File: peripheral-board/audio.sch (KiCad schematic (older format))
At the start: 4 parts, among them J6001 JACK_TRS_6PINS, U6001 TCA0372, U6002 MCP4011, U6003 MCP4011

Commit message: added audio jack
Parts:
- removed J6001: JACK_TRS_6PINS, symbol JACK_TRS_6PINS
- added J6001: FCR1295, lib:FCR1295, symbol FCR1295
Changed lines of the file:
@@
 $Descr A4 11693 8268
 encoding utf-8
-Sheet 6 10
+Sheet 7 10
 Title ""
 Date ""
@@
 Comment4 ""
 $EndDescr
-$Comp
-L JACK_TRS_6PINS J6001
-U 1 1 5819EF20
-P 6450 1700
-F 0 "J6001" H 6431 2225 50  0000 C CNN
-F 1 "JACK_TRS_6PINS" H 6431 2134 50  0000 C CNN
-F 2 "" H 6550 1550 50  0001 C CNN
-F 3 "" H 6550 1550 50  0000 C CNN
-	1    6450 1700
-	1    0    0    -1
-$EndComp
 $Comp
 L TCA0372 U6001
@@
 	1900 4750 1600 4750
 $Comp
-L GND #PWR028
+L GND #PWR054
 U 1 1 5823647F
 P 3300 3450
-F 0 "#PWR028" H 3300 3200 50  0001 C CNN
+F 0 "#PWR054" H 3300 3200 50  0001 C CNN
 F 1 "GND" H 3305 3277 50  0000 C CNN
 F 2 "" H 3300 3450 50  0000 C CNN
@@
 $EndComp
 $Comp
-L GND #PWR029
+L GND #PWR055
 U 1 1 582364AF
 P 3300 4850
-F 0 "#PWR029" H 3300 4600 50  0001 C CNN
+F 0 "#PWR055" H 3300 4600 50  0001 C CNN
 F 1 "GND" H 3305 4677 50  0000 C CNN
 F 2 "" H 3300 4850 50  0000 C CNN
@@
 $EndComp
 $Comp
-L +3V3 #PWR030
+L +3V3 #PWR056
 U 1 1 582364E9
 P 3300 2350
-F 0 "#PWR030" H 3300 2200 50  0001 C CNN
+F 0 "#PWR056" H 3300 2200 50  0001 C CNN
 F 1 "+3V3" V 3315 2478 50  0000 L CNN
 F 2 "" H 3300 2350 50  0000 C CNN
@@
 $EndComp
 $Comp
-L +3V3 #PWR031
+L +3V3 #PWR057
 U 1 1 58236543
 P 3350 3800
-F 0 "#PWR031" H 3350 3650 50  0001 C CNN
+F 0 "#PWR057" H 3350 3650 50  0001 C CNN
 F 1 "+3V3" V 3365 3928 50  0000 L CNN
 F 2 "" H 3350 3800 50  0000 C CNN
@@
 	4100 2800 4050 2800
 $Comp
-L GND #PWR032
+L GND #PWR058
 U 1 1 58240DA5
 P 4100 3050
-F 0 "#PWR032" H 4100 2800 50  0001 C CNN
+F 0 "#PWR058" H 4100 2800 50  0001 C CNN
 F 1 "GND" H 4105 2877 50  0000 C CNN
 F 2 "" H 4100 3050 50  0000 C CNN
@@
 $EndComp
 $Comp
-L GND #PWR033
+L GND #PWR059
 U 1 1 58240DD7
 P 4100 4450
-F 0 "#PWR033" H 4100 4200 50  0001 C CNN
+F 0 "#PWR059" H 4100 4200 50  0001 C CNN
 F 1 "GND" H 4105 4277 50  0000 C CNN
 F 2 "" H 4100 4450 50  0000 C CNN
@@
 Wire Wire Line
 	4100 3000 4100 3050
+$Comp
+L FCR1295 J6001
+U 1 1 589D4F61
+P 6450 1700
+F 0 "J6001" H 6431 2225 50  0000 C CNN
+F 1 "FCR1295" H 6431 2134 50  0000 C CNN
+F 2 "lib:FCR1295" H -800 400 50  0001 C CNN
+F 3 "" H -800 400 50  0001 C CNN
+	1    6450 1700
+	1    0    0    -1
+$EndComp
 $EndSCHEMATC

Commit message: added loudspeaker
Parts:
- added LS?: Speaker L, symbol Speaker
- added LS?: Speaker R, symbol Speaker
- added R?: R, symbol R
- added U? (x2): TL072, symbol TL072
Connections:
- wire segments 21 -> 27
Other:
- moved on the sheet: J6001
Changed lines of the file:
@@
 Wire Wire Line
 	3300 4800 3300 4850
-Text HLabel 6950 1400 2    60   Output ~ 0
+Text HLabel 8300 3300 0    60   Output ~ 0
 DETECT
 Wire Wire Line
-	6950 1400 6850 1400
+	8300 3300 8600 3300
 Wire Wire Line
 	4100 4200 4050 4200
@@
 L FCR1295 J6001
 U 1 1 589D4F61
-P 6450 1700
-F 0 "J6001" H 6431 2225 50  0000 C CNN
-F 1 "FCR1295" H 6431 2134 50  0000 C CNN
-F 2 "lib:FCR1295" H -800 400 50  0001 C CNN
-F 3 "" H -800 400 50  0001 C CNN
-	1    6450 1700
+P 9000 3600
+F 0 "J6001" H 8981 4125 50  0000 C CNN
+F 1 "FCR1295" H 8981 4034 50  0000 C CNN
+F 2 "lib:FCR1295" H 1750 2300 50  0001 C CNN
+F 3 "" H 1750 2300 50  0001 C CNN
+	1    9000 3600
+	-1   0    0    -1
+$EndComp
+$Comp
+L Speaker LS?
+U 1 1 58A1A3A1
+P 8750 2750
+F 0 "LS?" H 8714 2333 50  0000 C CNN
+F 1 "Speaker L" H 8714 2424 50  0000 C CNN
+F 2 "" H 250 1600 50  0001 C CNN
+F 3 "" H 240 1750 50  0001 C CNN
+	1    8750 2750
+	1    0    0    1
+$EndComp
+$Comp
+L Speaker LS?
+U 1 1 58A1A483
+P 8750 4400
+F 0 "LS?" H 8920 4396 50  0000 L CNN
+F 1 "Speaker R" H 8920 4305 50  0000 L CNN
+F 2 "" H 250 3250 50  0001 C CNN
+F 3 "" H 240 3400 50  0001 C CNN
+	1    8750 4400
 	1    0    0    -1
 $EndComp
+Wire Wire Line
+	7850 2750 8550 2750
+Wire Wire Line
+	7850 2750 7850 3500
+Wire Wire Line
+	7850 3500 8600 3500
+$Comp
+L GND #PWR?
+U 1 1 58A1A8BA
+P 8600 3400
+F 0 "#PWR?" H 8650 3450 50  0001 C CNN
+F 1 "GND" V 8605 3272 50  0000 R CNN
+F 2 "" H -250 200 50  0001 C CNN
+F 3 "" H -250 200 50  0001 C CNN
+	1    8600 3400
+	0    1    1    0
+$EndComp
+$Comp
+L +3V3 #PWR?
+U 1 1 58A1A914
+P 8500 3000
+F 0 "#PWR?" H 8550 3050 50  0001 C CNN
+F 1 "+3V3" V 8515 3128 50  0000 L CNN
+F 2 "" H 100 -100 50  0001 C CNN
+F 3 "" H 100 -100 50  0001 C CNN
+	1    8500 3000
+	0    -1   -1   0
+$EndComp
+$Comp
+L R R?
+U 1 1 58A1A952
+P 8500 3150
+F 0 "R?" H 8570 3196 50  0000 L CNN
+F 1 "R" H 8570 3105 50  0000 L CNN
+F 2 "" V -170 0   50  0001 C CNN
+F 3 "" H -100 0   50  0001 C CNN
+	1    8500 3150
+	1    0    0    -1
+$EndComp
+Connection ~ 8500 3300
+Wire Wire Line
+	8550 4400 7850 4400
+Wire Wire Line
+	7850 4400 7850 3700
+Wire Wire Line
+	7850 3700 8600 3700
+$Comp
+L GND #PWR?
+U 1 1 58A1ACEA
+P 8550 4500
+F 0 "#PWR?" H 8600 4550 50  0001 C CNN
+F 1 "GND" V 8555 4372 50  0000 R CNN
+F 2 "" H -850 1650 50  0001 C CNN
+F 3 "" H -850 1650 50  0001 C CNN
+	1    8550 4500
+	0    1    1    0
+$EndComp
+$Comp
+L GND #PWR?
+U 1 1 58A1AD9C
+P 8550 2650
+F 0 "#PWR?" H 8600 2700 50  0001 C CNN
+F 1 "GND" V 8555 2522 50  0000 R CNN
+F 2 "" H 100 300 50  0001 C CNN
+F 3 "" H 100 300 50  0001 C CNN
+	1    8550 2650
+	0    1    1    0
+$EndComp
+$Comp
+L TL072 U?
+U 1 1 58A1AFDE
+P 4000 6450
+F 0 "U?" H 4341 6496 50  0000 L CNN
+F 1 "TL072" H 4341 6405 50  0000 L CNN
+F 2 "" H -1950 5900 50  0001 C CNN
+F 3 "" H -1950 5900 50  0001 C CNN
+	1    4000 6450
+	1    0    0    -1
+$EndComp
+$Comp
+L TL072 U?
+U 2 1 58A1B0B3
+P 5100 6450
+F 0 "U?" H 5441 6496 50  0000 L CNN
+F 1 "TL072" H 5441 6405 50  0000 L CNN
+F 2 "" H -850 5900 50  0001 C CNN
+F 3 "" H -850 5900 50  0001 C CNN
+	2    5100 6450
+	1    0    0    -1
+$EndComp

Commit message: audio circuitry
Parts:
- removed U6001: TCA0372, Housings_SOIC:SOIC-16_7.5x10.3mm_Pitch1.27mm, symbol TCA0372
- removed U? (x2): TL072, symbol TL072
- added C7001, C7002: 100n, symbol C
- added C7004, C7011: 100u, Capacitors_Tantalum_SMD:CP_Tantalum_Case-D_EIA-7343-31_Reflow, symbol CP
- added C7005, C7012: 100n, Capacitors_SMD:C_0805, symbol C
- added C7006, C7007, C7013, C7014: 1u, Capacitors_SMD:C_0805, symbol C
- added C7008, C7015: 220u, Capacitors_Tantalum_SMD:CP_Tantalum_Case-D_EIA-7343-31_Reflow, symbol CP
- added C7009, C7016: 1n, Capacitors_SMD:C_0805, symbol C
- added C7010, C7017: 47n, Capacitors_SMD:C_0805, symbol C
- added R7003, R7007: 100k, Resistors_SMD:R_0805, symbol R
- added R7004, R7008: 10k, Resistors_SMD:R_0805, symbol R
- added R7006, R7009: 10, Resistors_SMD:R_0805, symbol R
- added U7001, U7002: LM386, Housings_SOIC:SOIC-8_3.9x4.9mm_Pitch1.27mm, symbol LM386
- LS7001, LS7002: renamed from LS?; footprint (none) -> Socket_Strips:Socket_Strip_Straight_1x02_Pitch2.54mm
- R7005: renamed from R?; value R -> 100k; footprint (none) -> Resistors_SMD:R_0805
- renumbered J6001 to J7001, U6002 to U7003, U6003 to U7004
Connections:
- net labels added: +BATT, JACK_L, JACK_R, SPKR_L, SPKR_R
- wire segments 27 -> 63
- no-connect marks 0 -> 4
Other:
- moved on the sheet: J7001, LS7001, LS7002, R7005

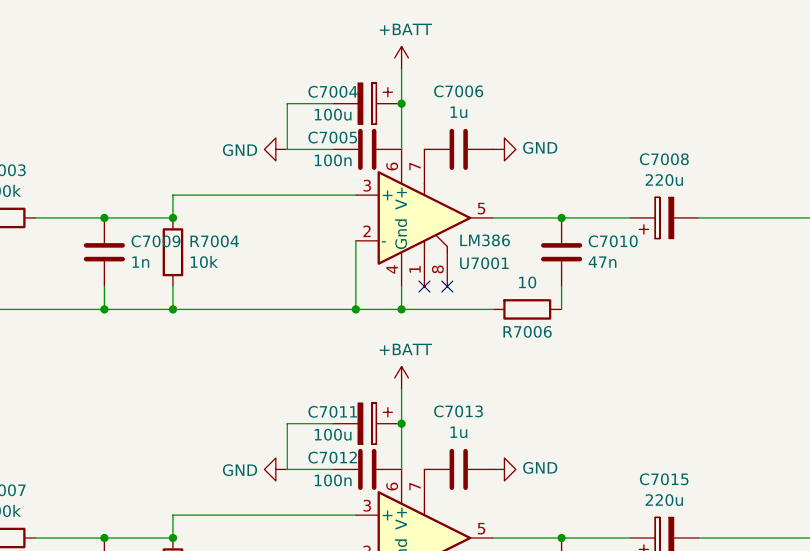
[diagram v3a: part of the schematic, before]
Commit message: power supply component placement
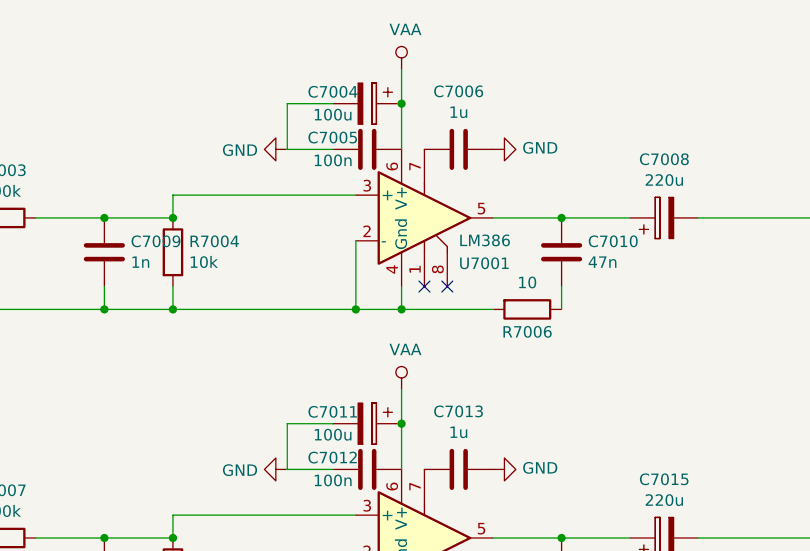
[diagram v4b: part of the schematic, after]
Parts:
- C7001, C7002: footprint (none) -> Capacitors_SMD:C_0805
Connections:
- net +BATT renamed VAA
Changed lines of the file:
@@
 NoConn ~ 6350 3200
-$Comp
-L +BATT #PWR7001
-U 1 1 58A358DE
-P 6250 2250
-F 0 "#PWR7001" H 6300 2300 50  0001 C CNN
-F 1 "+BATT" H 6265 2423 50  0000 C CNN
-F 2 "" H -1300 -650 50  0001 C CNN
-F 3 "" H -1300 -650 50  0001 C CNN
-	1    6250 2250
-	1    0    0    -1
-$EndComp
 $Comp
 L GND #PWR7005
@@
 Connection ~ 6250 2400
 $Comp
-L +BATT #PWR7011
-U 1 1 58A39047
-P 6250 3650
-F 0 "#PWR7011" H 6300 3700 50  0001 C CNN
-F 1 "+BATT" H 6265 3823 50  0000 C CNN
-F 2 "" H -1300 750 50  0001 C CNN
-F 3 "" H -1300 750 50  0001 C CNN
-	1    6250 3650
-	1    0    0    -1
-$EndComp
-$Comp
 L C C7012
 U 1 1 58A3904D
@@
 F 0 "C7001" V 2898 2350 50  0000 C CNN
 F 1 "100n" V 2989 2350 50  0000 C CNN
-F 2 "" H 338 400 50  0001 C CNN
+F 2 "Capacitors_SMD:C_0805" H 338 400 50  0001 C CNN
 F 3 "" H 300 550 50  0001 C CNN
 	1    3150 2350
@@
 F 0 "C7002" V 2898 3800 50  0000 C CNN
 F 1 "100n" V 2989 3800 50  0000 C CNN
-F 2 "" H 338 1850 50  0001 C CNN
+F 2 "Capacitors_SMD:C_0805" H 338 1850 50  0001 C CNN
 F 3 "" H 300 2000 50  0001 C CNN
 	1    3150 3800
@@
 	0    1    1    0
 $EndComp
+$Comp
+L VAA #PWR7001
+U 1 1 58A8FF55
+P 6250 2250
+F 0 "#PWR7001" H -2150 900 50  0001 C CNN
+F 1 "VAA" H 6267 2423 50  0000 C CNN
+F 2 "" H -2150 1050 50  0001 C CNN
+F 3 "" H -2150 1050 50  0001 C CNN
+	1    6250 2250
+	1    0    0    -1
+$EndComp
+$Comp
+L VAA #PWR7011
+U 1 1 58A9009E
+P 6250 3650
+F 0 "#PWR7011" H -2150 2300 50  0001 C CNN
+F 1 "VAA" H 6267 3823 50  0000 C CNN
+F 2 "" H -2150 2450 50  0001 C CNN
+F 3 "" H -2150 2450 50  0001 C CNN
+	1    6250 3650
+	1    0    0    -1
+$EndComp
 $EndSCHEMATC

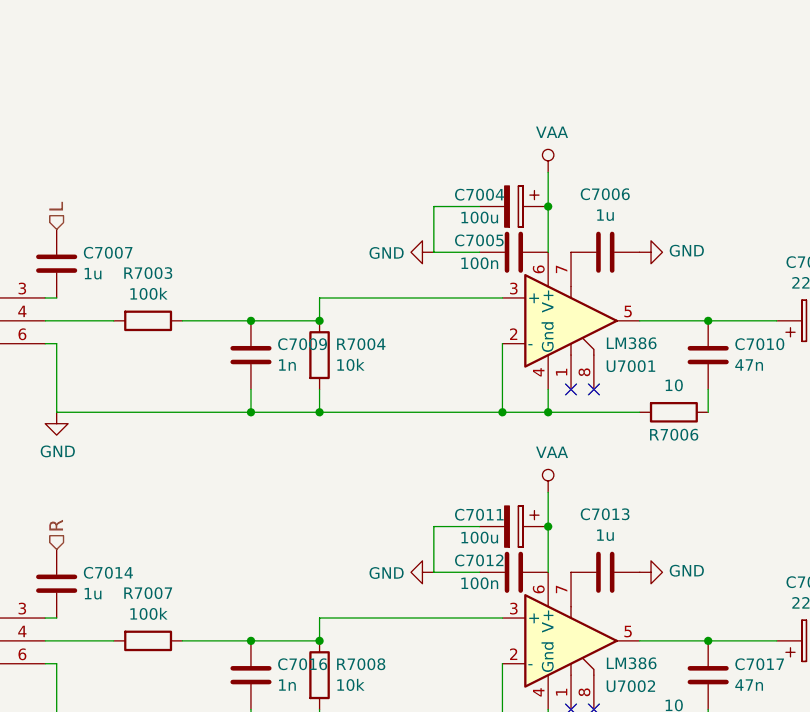
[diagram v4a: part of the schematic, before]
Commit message: audio components placement
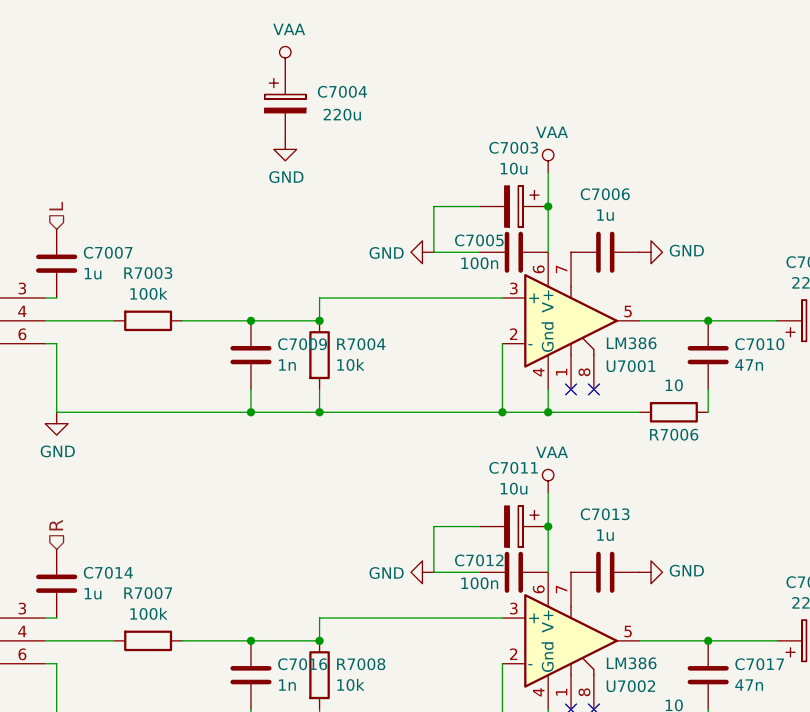
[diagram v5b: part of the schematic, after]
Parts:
- added C7003: 10u, Capacitors_SMD:c_elec_6.3x5.8, symbol CP
- C7004: value 100u -> 220u; footprint Capacitors_Tantalum_SMD:CP_Tantalum_Case-D_EIA-7343-31_Reflow -> Capacitors_SMD:c_elec_8x6.7
- C7008, C7015: footprint Capacitors_Tantalum_SMD:CP_Tantalum_Case-D_EIA-7343-31_Reflow -> Capacitors_SMD:c_elec_8x6.7
- C7011: value 100u -> 10u; footprint Capacitors_Tantalum_SMD:CP_Tantalum_Case-D_EIA-7343-31_Reflow -> Capacitors_SMD:c_elec_6.3x5.8
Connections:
- net GND: now also C7003.2
- net VAA: now also C7003.1
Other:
- moved on the sheet: C7004
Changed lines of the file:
@@
 $EndComp
 $Comp
-L GND #PWR7010
+L GND #PWR055
 U 1 1 5823647F
 P 3300 3450
-F 0 "#PWR7010" H 3300 3200 50  0001 C CNN
+F 0 "#PWR055" H 3300 3200 50  0001 C CNN
 F 1 "GND" H 3305 3277 50  0000 C CNN
 F 2 "" H 3300 3450 50  0000 C CNN
@@
 $EndComp
 $Comp
-L GND #PWR7018
+L GND #PWR056
 U 1 1 582364AF
 P 3300 4850
-F 0 "#PWR7018" H 3300 4600 50  0001 C CNN
+F 0 "#PWR056" H 3300 4600 50  0001 C CNN
 F 1 "GND" H 3305 4677 50  0000 C CNN
 F 2 "" H 3300 4850 50  0000 C CNN
@@
 $EndComp
 $Comp
-L +3V3 #PWR7003
+L +3V3 #PWR057
 U 1 1 582364E9
 P 3300 2350
-F 0 "#PWR7003" H 3300 2200 50  0001 C CNN
+F 0 "#PWR057" H 3300 2200 50  0001 C CNN
 F 1 "+3V3" V 3315 2478 50  0000 L CNN
 F 2 "" H 3300 2350 50  0000 C CNN
@@
 $EndComp
 $Comp
-L +3V3 #PWR7013
+L +3V3 #PWR058
 U 1 1 58236543
 P 3350 3800
-F 0 "#PWR7013" H 3350 3650 50  0001 C CNN
+F 0 "#PWR058" H 3350 3650 50  0001 C CNN
 F 1 "+3V3" V 3365 3928 50  0000 L CNN
 F 2 "" H 3350 3800 50  0000 C CNN
@@
 DETECT
 $Comp
-L GND #PWR7008
+L GND #PWR059
 U 1 1 58240DA5
 P 4100 3300
-F 0 "#PWR7008" H 4100 3050 50  0001 C CNN
+F 0 "#PWR059" H 4100 3050 50  0001 C CNN
 F 1 "GND" H 4105 3127 50  0000 C CNN
 F 2 "" H 4100 3300 50  0000 C CNN
@@
 $EndComp
 $Comp
-L GND #PWR7009
+L GND #PWR060
 U 1 1 58A1A8BA
 P 10050 3400
-F 0 "#PWR7009" H 10100 3450 50  0001 C CNN
+F 0 "#PWR060" H 10100 3450 50  0001 C CNN
 F 1 "GND" V 10055 3272 50  0000 R CNN
 F 2 "" H 1200 200 50  0001 C CNN
@@
 $EndComp
 $Comp
-L +3V3 #PWR7007
+L +3V3 #PWR061
 U 1 1 58A1A914
 P 9950 3000
-F 0 "#PWR7007" H 10000 3050 50  0001 C CNN
+F 0 "#PWR061" H 10000 3050 50  0001 C CNN
 F 1 "+3V3" V 9965 3128 50  0000 L CNN
 F 2 "" H 1550 -100 50  0001 C CNN
@@
 $EndComp
 $Comp
-L GND #PWR7016
+L GND #PWR062
 U 1 1 58A1ACEA
 P 10000 4500
-F 0 "#PWR7016" H 10050 4550 50  0001 C CNN
+F 0 "#PWR062" H 10050 4550 50  0001 C CNN
 F 1 "GND" V 10005 4372 50  0000 R CNN
 F 2 "" H 600 1650 50  0001 C CNN
@@
 $EndComp
 $Comp
-L GND #PWR7006
+L GND #PWR063
 U 1 1 58A1AD9C
 P 10000 2650
-F 0 "#PWR7006" H 10050 2700 50  0001 C CNN
+F 0 "#PWR063" H 10050 2700 50  0001 C CNN
 F 1 "GND" V 10005 2522 50  0000 R CNN
 F 2 "" H 1550 300 50  0001 C CNN
@@
 NoConn ~ 6350 3200
 $Comp
-L GND #PWR7005
+L GND #PWR064
 U 1 1 58A359F1
 P 6650 2600
-F 0 "#PWR7005" H -400 -250 50  0001 C CNN
+F 0 "#PWR064" H -400 -250 50  0001 C CNN
 F 1 "GND" V 6655 2472 50  0000 R CNN
 F 2 "" H -400 0   50  0001 C CNN
@@
 F 0 "C7008" V 7655 2900 50  0000 C CNN
 F 1 "220u" V 7564 2900 50  0000 C CNN
-F 2 "Capacitors_Tantalum_SMD:CP_Tantalum_Case-D_EIA-7343-31_Reflow" H 38  -150 50  0001 C CNN
+F 2 "Capacitors_SMD:c_elec_8x6.7" H 38  -150 50  0001 C CNN
 F 3 "" H 0   0   50  0001 C CNN
 	1    7400 2900
@@
 $EndComp
 $Comp
-L GND #PWR7004
+L GND #PWR065
 U 1 1 58A36C12
 P 5750 2600
-F 0 "#PWR7004" H -1400 250 50  0001 C CNN
+F 0 "#PWR065" H -1400 250 50  0001 C CNN
 F 1 "GND" V 5755 2472 50  0000 R CNN
 F 2 "" H -1400 500 50  0001 C CNN
@@
 	6250 2250 6250 2600
 $Comp
-L GND #PWR7017
+L GND #PWR066
 U 1 1 58A3787F
 P 4100 4700
-F 0 "#PWR7017" H 4100 4450 50  0001 C CNN
+F 0 "#PWR066" H 4100 4450 50  0001 C CNN
 F 1 "GND" H 4105 4527 50  0000 C CNN
 F 2 "" H 4100 4700 50  0000 C CNN
@@
 NoConn ~ 6350 4600
 $Comp
-L GND #PWR7015
+L GND #PWR067
 U 1 1 58A378BA
 P 6650 4000
-F 0 "#PWR7015" H -400 1150 50  0001 C CNN
+F 0 "#PWR067" H -400 1150 50  0001 C CNN
 F 1 "GND" V 6655 3872 50  0000 R CNN
 F 2 "" H -400 1400 50  0001 C CNN
@@
 F 0 "C7015" V 7655 4300 50  0000 C CNN
 F 1 "220u" V 7564 4300 50  0000 C CNN
-F 2 "Capacitors_Tantalum_SMD:CP_Tantalum_Case-D_EIA-7343-31_Reflow" H 38  1250 50  0001 C CNN
+F 2 "Capacitors_SMD:c_elec_8x6.7" H 38  1250 50  0001 C CNN
 F 3 "" H 0   1400 50  0001 C CNN
 	1    7400 4300
@@
 L CP C7004
 U 1 1 58A38863
-P 6100 2400
-F 0 "C7004" V 6050 2250 50  0000 C CNN
-F 1 "100u" V 6150 2250 50  0000 C CNN
-F 2 "Capacitors_Tantalum_SMD:CP_Tantalum_Case-D_EIA-7343-31_Reflow" H -1862 -100 50  0001 C CNN
-F 3 "" H -1900 50  50  0001 C CNN
-	1    6100 2400
-	0    1    1    0
+P 5100 1950
+F 0 "C7004" H 5350 2000 50  0000 C CNN
+F 1 "220u" H 5350 1900 50  0000 C CNN
+F 2 "Capacitors_SMD:c_elec_8x6.7" H -2862 -550 50  0001 C CNN
+F 3 "" H -2900 -400 50  0001 C CNN
+	1    5100 1950
+	1    0    0    -1
 $EndComp
 Wire Wire Line
@@
 $EndComp
 $Comp
-L GND #PWR7014
+L GND #PWR068
 U 1 1 58A39053
 P 5750 4000
-F 0 "#PWR7014" H -1400 1650 50  0001 C CNN
+F 0 "#PWR068" H -1400 1650 50  0001 C CNN
 F 1 "GND" V 5755 3872 50  0000 R CNN
 F 2 "" H -1400 1900 50  0001 C CNN
@@
 Wire Wire Line
 	6250 3650 6250 4000
-$Comp
-L CP C7011
-U 1 1 58A3905A
-P 6100 3800
-F 0 "C7011" V 6050 3650 50  0000 C CNN
-F 1 "100u" V 6150 3650 50  0000 C CNN
-F 2 "Capacitors_Tantalum_SMD:CP_Tantalum_Case-D_EIA-7343-31_Reflow" H -1862 1300 50  0001 C CNN
-F 3 "" H -1900 1450 50  0001 C CNN
-	1    6100 3800
-	0    1    1    0
-$EndComp
 Wire Wire Line
 	5950 3800 5750 3800
@@
 $EndComp
 $Comp
-L GND #PWR7002
+L GND #PWR069
 U 1 1 58A3B2B9
 P 3000 2350
-F 0 "#PWR7002" H 50  -50 50  0001 C CNN
+F 0 "#PWR069" H 50  -50 50  0001 C CNN
 F 1 "GND" V 3005 2222 50  0000 R CNN
 F 2 "" H 50  200 50  0001 C CNN
@@
 $EndComp
 $Comp
-L GND #PWR7012
+L GND #PWR070
 U 1 1 58A3B4D5
 P 3000 3800
-F 0 "#PWR7012" H 50  1400 50  0001 C CNN
+F 0 "#PWR070" H 50  1400 50  0001 C CNN
 F 1 "GND" V 3005 3672 50  0000 R CNN
 F 2 "" H 50  1650 50  0001 C CNN
@@
 $EndComp
 $Comp
-L VAA #PWR7001
+L VAA #PWR071
 U 1 1 58A8FF55
 P 6250 2250
-F 0 "#PWR7001" H -2150 900 50  0001 C CNN
+F 0 "#PWR071" H -2150 900 50  0001 C CNN
 F 1 "VAA" H 6267 2423 50  0000 C CNN
 F 2 "" H -2150 1050 50  0001 C CNN
@@
 $EndComp
 $Comp
-L VAA #PWR7011
+L VAA #PWR072
 U 1 1 58A9009E
 P 6250 3650
-F 0 "#PWR7011" H -2150 2300 50  0001 C CNN
+F 0 "#PWR072" H -2150 2300 50  0001 C CNN
 F 1 "VAA" H 6267 3823 50  0000 C CNN
 F 2 "" H -2150 2450 50  0001 C CNN
@@
 	1    0    0    -1
 $EndComp
+$Comp
+L CP C7003
+U 1 1 58A4CC88
+P 6100 2400
+F 0 "C7003" V 5845 2400 50  0000 C CNN
+F 1 "10u" V 5936 2400 50  0000 C CNN
+F 2 "Capacitors_SMD:c_elec_6.3x5.8" H -1812 400 50  0001 C CNN
+F 3 "" H -1850 550 50  0001 C CNN
+	1    6100 2400
+	0    1    1    0
+$EndComp
+$Comp
+L CP C7011
+U 1 1 58A4CE56
+P 6100 3800
+F 0 "C7011" V 5845 3800 50  0000 C CNN
+F 1 "10u" V 5936 3800 50  0000 C CNN
+F 2 "Capacitors_SMD:c_elec_6.3x5.8" H -1812 1800 50  0001 C CNN
+F 3 "" H -1850 1950 50  0001 C CNN
+	1    6100 3800
+	0    1    1    0
+$EndComp
+$Comp
+L VAA #PWR073
+U 1 1 58A4CF7D
+P 5100 1800
+F 0 "#PWR073" H -3300 450 50  0001 C CNN
+F 1 "VAA" H 5117 1973 50  0000 C CNN
+F 2 "" H -3300 600 50  0001 C CNN
+F 3 "" H -3300 600 50  0001 C CNN
+	1    5100 1800
+	1    0    0    -1
+$EndComp
+$Comp
+L GND #PWR074
+U 1 1 58A4D14E
+P 5100 2100
+F 0 "#PWR074" H 5100 1850 50  0001 C CNN
+F 1 "GND" H 5105 1927 50  0000 C CNN
+F 2 "" H 5100 2100 50  0000 C CNN
+F 3 "" H 5100 2100 50  0000 C CNN
+	1    5100 2100
+	1    0    0    -1
+$EndComp
